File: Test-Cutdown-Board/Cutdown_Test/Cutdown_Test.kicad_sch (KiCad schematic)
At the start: 29 parts, among them J2 Conn_01x02_Socket, J4 Nichrome, SW1 SW_SPDT, U1 LT3120JV-PBF

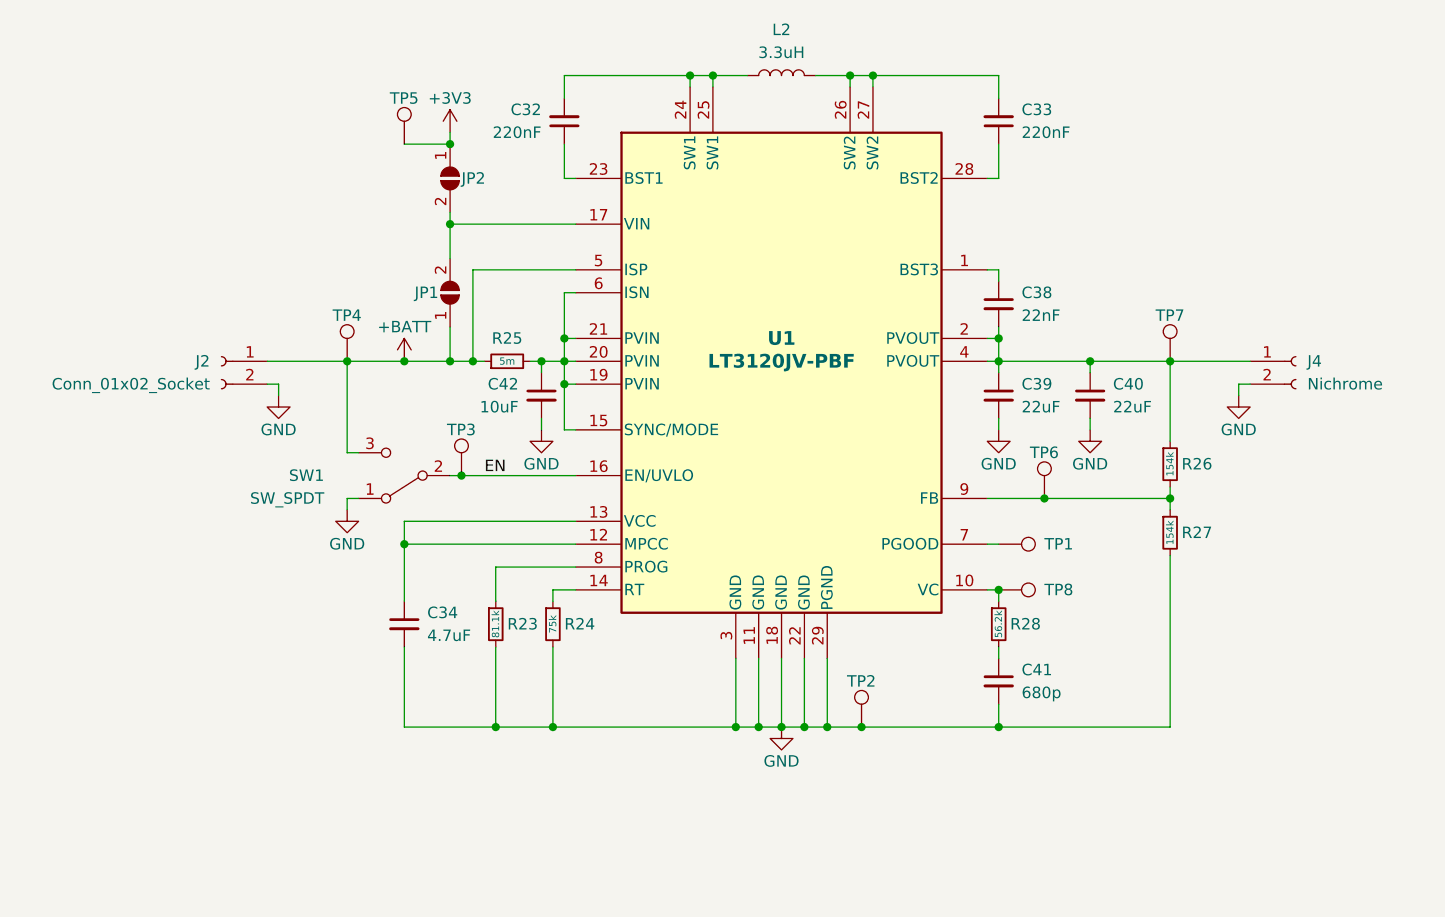
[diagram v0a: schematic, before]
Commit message: ready to order Cutdown Test
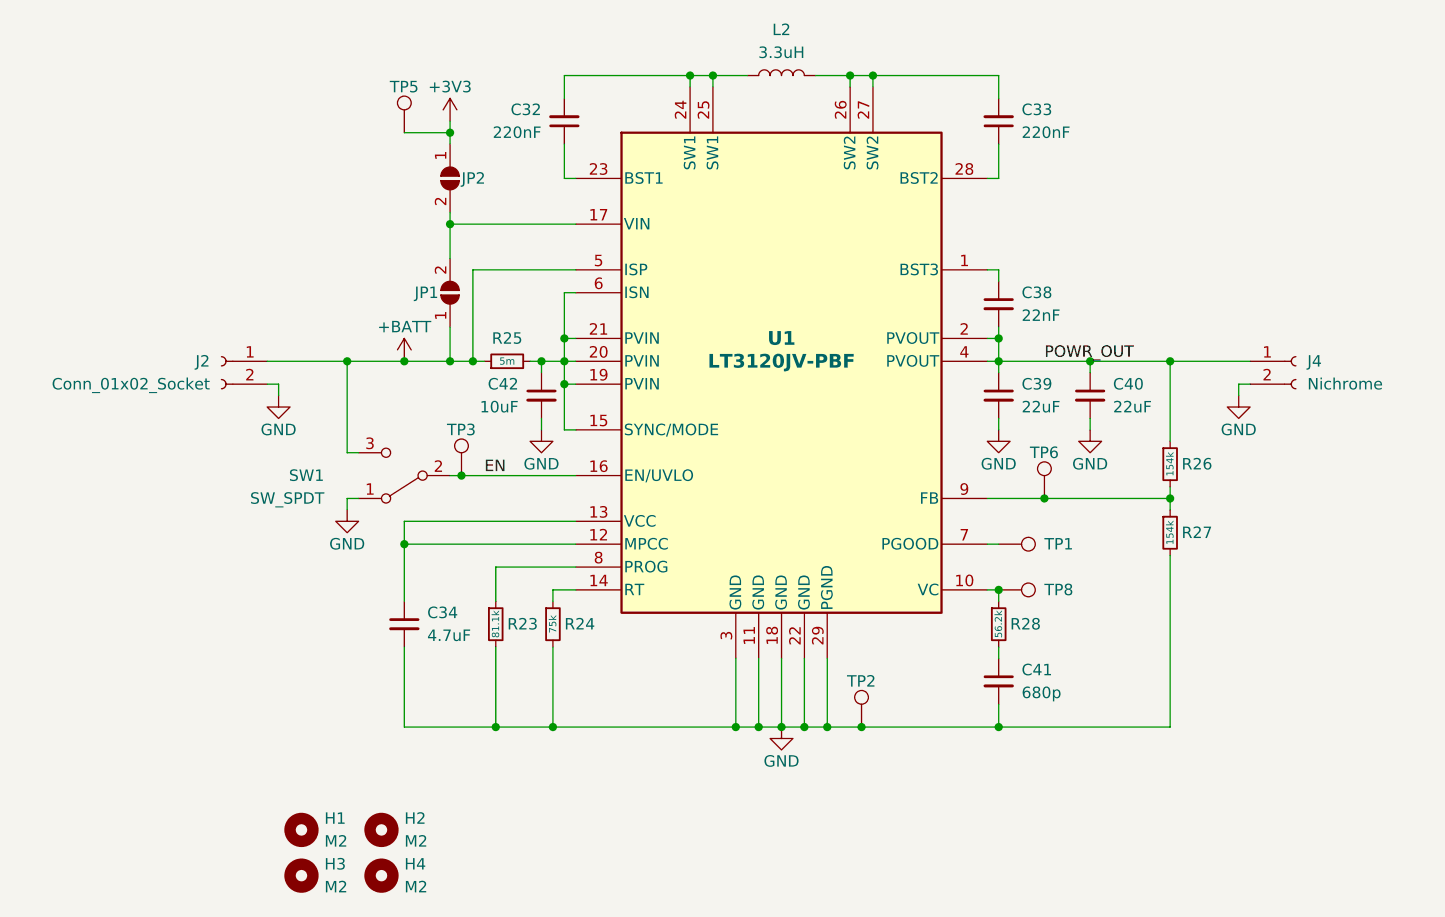
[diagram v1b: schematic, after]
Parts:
- removed TP4, TP7: TestPoint, TestPoint:TestPoint_Keystone_5000-5004_Miniature, symbol Connector:TestPoint
- added H1, H2, H3, H4: M2, MountingHole:MountingHole_2.2mm_M2, symbol Mechanical:MountingHole
- R25: footprint (none) -> Resistor_SMD:R_2512_6332Metric
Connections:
- net POWR_OUT: now reaches C38.2, C39.1, C40.1, J4.1 (Pin_1), R26.1, U1.2 (PVOUT), U1.4 (PVOUT)
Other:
- moved on the sheet: TP5

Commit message: minor cutdown circuit tuning
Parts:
- R23: value 81.1k -> 57.4k
- R26: value 154k -> 277k
- R27: value 154k -> 100k
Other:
- moved on the sheet: J4
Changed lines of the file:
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@@
   (junction (at 125.73 127) (diameter 0) (color 0 0 0 0)
   )
-  (wire (pts (xy 181.61 90.17) (xy 181.61 88.9))
+  (wire (pts (xy 184.15 90.17) (xy 184.15 88.9))
     (stroke (width 0) (type default))
   )
@@
     (stroke (width 0) (type default))
   )
-  (wire (pts (xy 173.99 86.36) (xy 182.88 86.36))
+  (wire (pts (xy 173.99 86.36) (xy 185.42 86.36))
     (stroke (width 0) (type default))
   )
@@
     (stroke (width 0) (type default))
   )
-  (wire (pts (xy 181.61 88.9) (xy 182.88 88.9))
+  (wire (pts (xy 184.15 88.9) (xy 185.42 88.9))
     (stroke (width 0) (type default))
   )
@@
     (stroke (width 0) (type default))
   )
-  (label "POWR_OUT" (at 160.02 86.36 0) (fields_autoplaced)
+  (label "POWR_OUT" (at 173.99 86.36 0) (fields_autoplaced)
     (effects (font (size 1.27 1.27)) (justify left bottom))
   )
@@
     )
   )
-  (symbol (lib_name "GND_16") (lib_id "power:GND") (at 181.61 90.17 0) (unit 1)
-    (in_bom yes) (on_board yes) (dnp no)
-    (property "Reference" "#PWR057" (at 181.61 96.52 0)
-      (effects (font (size 1.27 1.27)) hide)
-    )
-    (property "Value" "GND" (at 181.61 93.98 0)
+  (symbol (lib_name "GND_16") (lib_id "power:GND") (at 184.15 90.17 0) (unit 1)
+    (in_bom yes) (on_board yes) (dnp no)
+    (property "Reference" "#PWR057" (at 184.15 96.52 0)
+      (effects (font (size 1.27 1.27)) hide)
+    )
+    (property "Value" "GND" (at 184.15 93.98 0)
       (effects (font (size 1.27 1.27)))
     )
-    (property "Footprint" "" (at 181.61 90.17 0)
-      (effects (font (size 1.27 1.27)) hide)
-    )
-    (property "Datasheet" "" (at 181.61 90.17 0)
+    (property "Footprint" "" (at 184.15 90.17 0)
+      (effects (font (size 1.27 1.27)) hide)
+    )
+    (property "Datasheet" "" (at 184.15 90.17 0)
       (effects (font (size 1.27 1.27)) hide)
     )
@@
       (effects (font (size 1.27 1.27)) (justify left))
     )
-    (property "Value" "154k" (at 173.99 97.79 90)
+    (property "Value" "277k" (at 173.99 97.79 90)
       (effects (font (size 0.8 0.8)))
     )
@@
       (effects (font (size 1.27 1.27)) (justify left))
     )
-    (property "Value" "154k" (at 173.99 105.41 90)
+    (property "Value" "100k" (at 173.99 105.41 90)
       (effects (font (size 0.8 0.8)))
     )
@@
       (effects (font (size 1.27 1.27)) (justify left))
     )
-    (property "Value" "81.1k" (at 99.06 115.57 90)
+    (property "Value" "57.4k" (at 99.06 115.57 90)
       (effects (font (size 0.8 0.8)))
     )
@@
     )
   )
-  (symbol (lib_id "Connector:Conn_01x02_Socket") (at 187.96 86.36 0) (unit 1)
+  (symbol (lib_id "Connector:Conn_01x02_Socket") (at 190.5 86.36 0) (unit 1)
     (in_bom yes) (on_board yes) (dnp no) (fields_autoplaced)
-    (property "Reference" "J4" (at 189.23 86.36 0)
-      (effects (font (size 1.27 1.27)) (justify left))
-    )
-    (property "Value" "Nichrome" (at 189.23 88.9 0)
-      (effects (font (size 1.27 1.27)) (justify left))
-    )
-    (property "Footprint" "Connector_PinHeader_2.54mm:PinHeader_1x02_P2.54mm_Vertical" (at 187.96 86.36 0)
-      (effects (font (size 1.27 1.27)) hide)
-    )
-    (property "Datasheet" "~" (at 187.96 86.36 0)
-      (effects (font (size 1.27 1.27)) hide)
-    )
+    (property "Reference" "J4" (at 191.77 86.36 0)
+      (effects (font (size 1.27 1.27)) (justify left))
+    )
+    (property "Value" "Nichrome" (at 191.77 88.9 0)
+      (effects (font (size 1.27 1.27)) (justify left))
+    )
+    (property "Footprint" "Connector_PinHeader_2.54mm:PinHeader_1x02_P2.54mm_Vertical" (at 190.5 86.36 0)
+      (effects (font (size 1.27 1.27)) hide)
+    )
+    (property "Datasheet" "~" (at 190.5 86.36 0)
+      (effects (font (size 1.27 1.27)) hide)
+    )

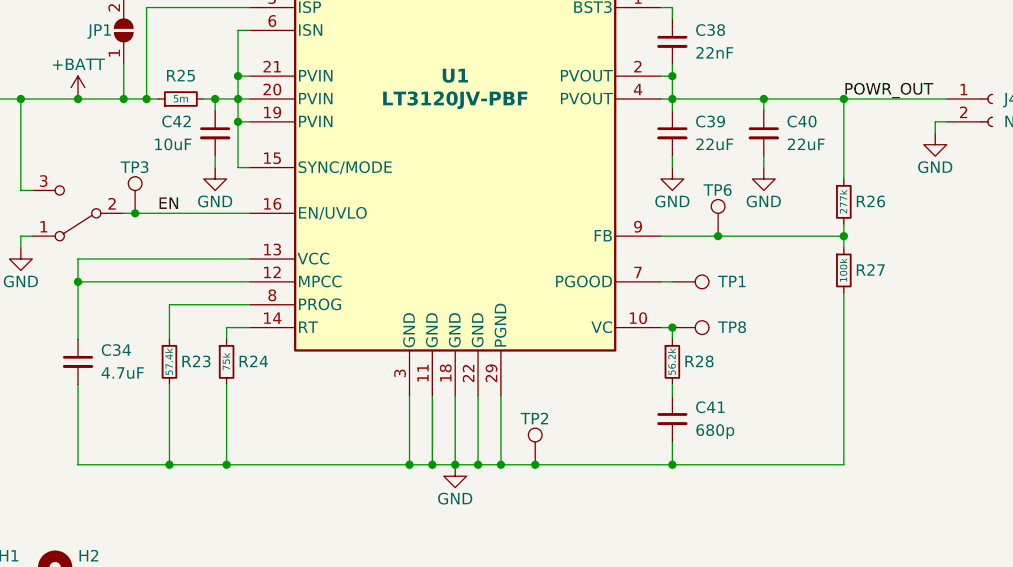
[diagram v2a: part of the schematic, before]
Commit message: ordered cutdown test board, more work on Babel fish
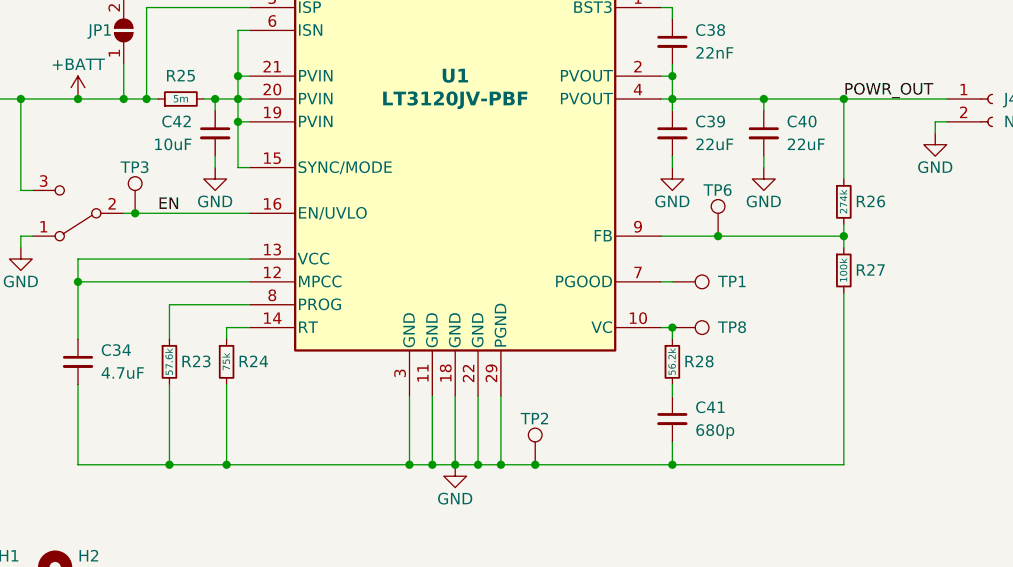
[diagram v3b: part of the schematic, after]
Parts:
- R23: value 57.4k -> 57.6k
- R26: value 277k -> 274k
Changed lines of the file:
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@@
       (effects (font (size 1.27 1.27)) (justify left))
     )
-    (property "Value" "277k" (at 173.99 97.79 90)
+    (property "Value" "274k" (at 173.99 97.79 90)
       (effects (font (size 0.8 0.8)))
     )
@@
       (effects (font (size 1.27 1.27)) (justify left))
     )
-    (property "Value" "57.4k" (at 99.06 115.57 90)
+    (property "Value" "57.6k" (at 99.06 115.57 90)
       (effects (font (size 0.8 0.8)))
     )
